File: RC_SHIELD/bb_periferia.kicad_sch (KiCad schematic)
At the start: 29 parts, among them J1 P5a, J2 P4a, J3 FAN, J4 I2C_TEMP, J5 GPIO1, J6 ESTOP, J7 DOOR_SWITCH, J8 GPIO2, J9 SPI, Q1 BSS123, Q2 BSS123, U1 ESP8266-01/ESP-01, U2 SN75LBC179AD, U3 LCD-016N002L

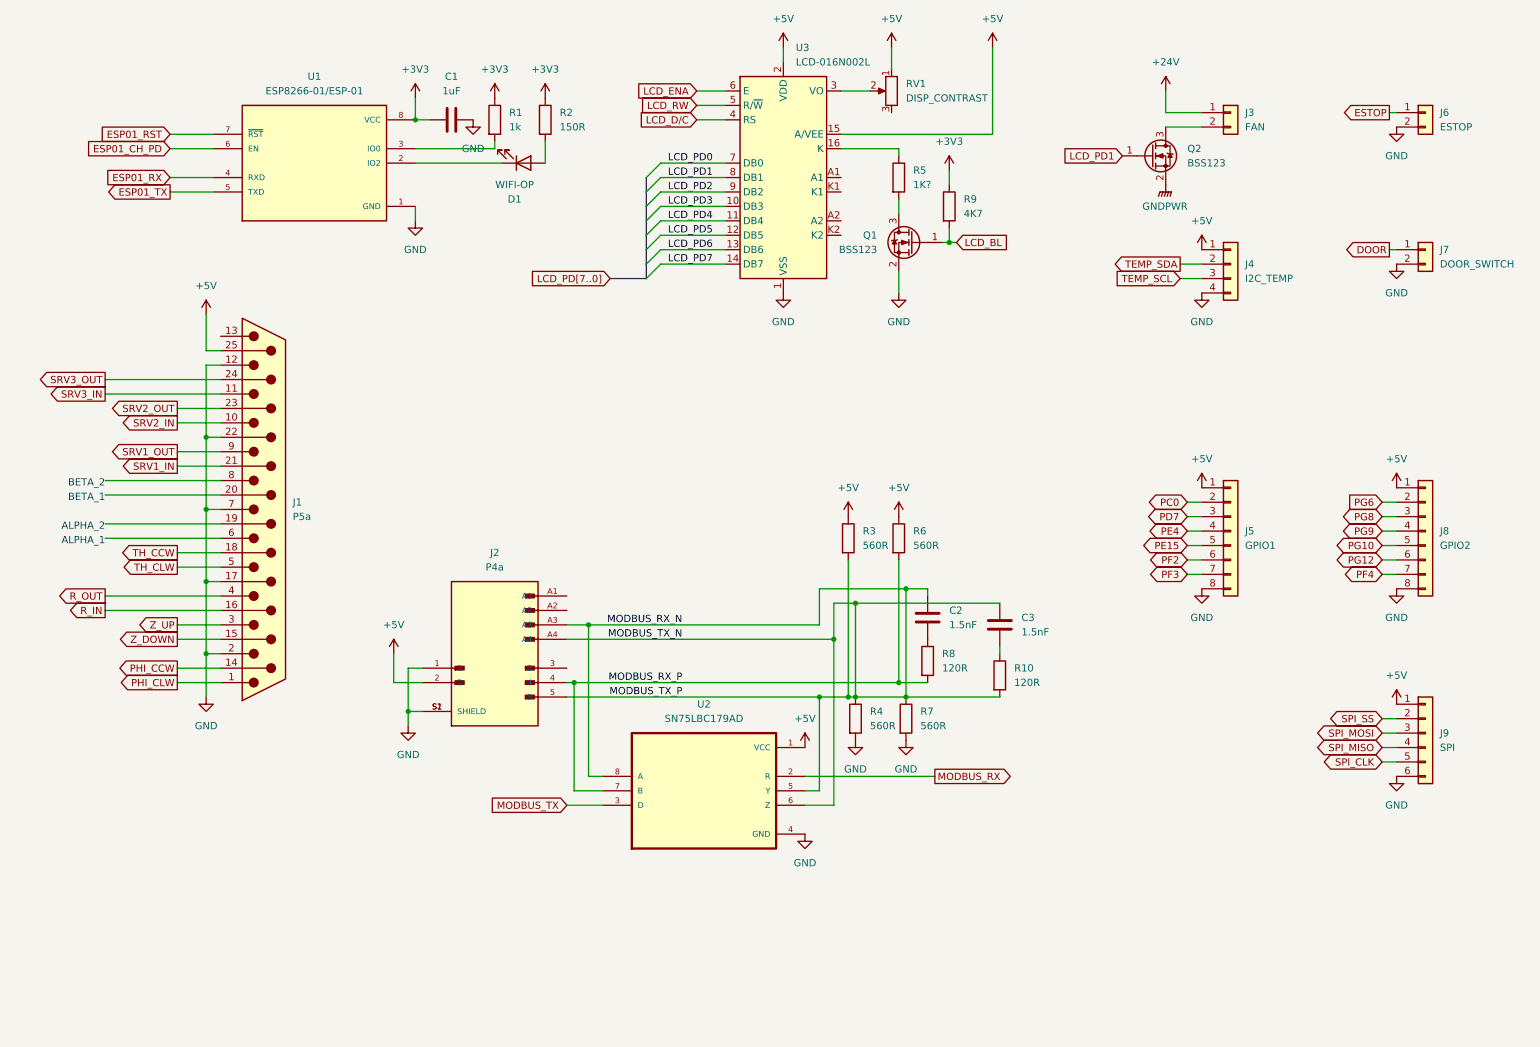
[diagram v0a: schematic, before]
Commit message: added secondary MCU to schematic and made it more consistent
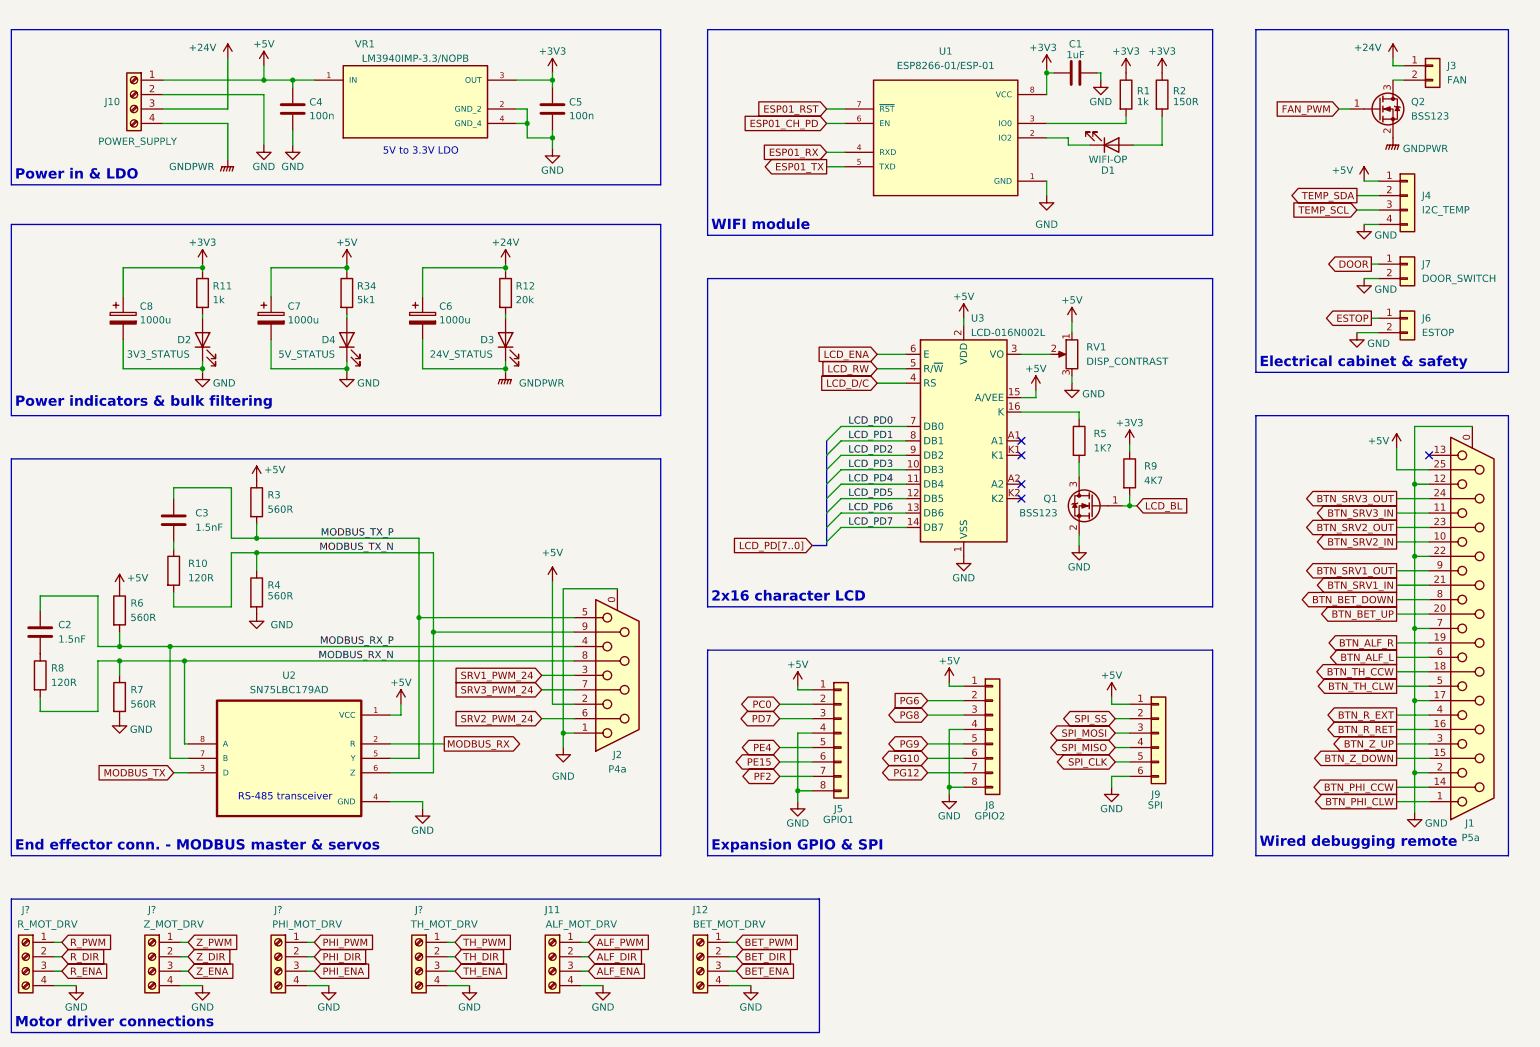
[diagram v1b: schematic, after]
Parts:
- added C4, C5: 100n, symbol Device:C
- added C6, C7, C8: 1000u, symbol Device:C_Polarized
- added D2: 3V3_STATUS, symbol Device:LED
- added D3: 24V_STATUS, symbol Device:LED
- added D4: 5V_STATUS, symbol Device:LED
- added J10: POWER_SUPPLY, symbol Connector:Screw_Terminal_01x04
- added J11: ALF_MOT_DRV, symbol Connector:Screw_Terminal_01x04
- added J12: BET_MOT_DRV, symbol Connector:Screw_Terminal_01x04
- added J?: TH_MOT_DRV, symbol Connector:Screw_Terminal_01x04
- added J?: PHI_MOT_DRV, symbol Connector:Screw_Terminal_01x04
- added J?: Z_MOT_DRV, symbol Connector:Screw_Terminal_01x04
- added J?: R_MOT_DRV, symbol Connector:Screw_Terminal_01x04
- added R11: 1k, symbol Device:R
- added R12: 20k, symbol Device:R
- added R34: 5k1, symbol Device:R
- added VR1: LM3940IMP-3.3/NOPB, LM3940IMP-3.3/NOPB:VREG_LM3940IMP-3.3/NOPB, symbol LM3940IMP-3.3_NOPB:LM3940IMP-3.3/NOPB
- J1: symbol Connector:DB25_Plug -> Connector:DB25_Receptacle_MountingHoles
- J2: symbol DB9W4P500H30LF:DB9W4P500H30LF -> Connector:DE9_Receptacle_MountingHoles
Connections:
- net PF3 is gone; now on net PF2: J5.7 (Pin_7)
- net PF4 is gone; now on net PG12: J8.7 (Pin_7)
- net +24V: now also C6.1, J10.3 (Pin_3), R12.1
- net +3V3: now also C5.1, C8.1, R11.1, VR1.3 (OUT)
- net +5V: now also C4.1, C7.1, J10.1 (Pin_1), R34.1, VR1.1 (IN)
- net GND: now also J1.0 (PAD), J2.0 (PAD), J5.4 (Pin_4), J8.4 (Pin_4), RV1.3, C4.2, C5.2, C7.2, C8.2, D2.1 (K), D4.1 (K), J10.2 (Pin_2), J11.4 (Pin_4), J12.4 (Pin_4), J?.4 (Pin_4), J?.4 (Pin_4), J?.4 (Pin_4), J?.4 (Pin_4), VR1.2 (GND_2), VR1.4 (GND_4); no longer J2.S1 (SHIELD), J2.S2 (SHIELD)
- net GNDPWR: now also C6.2, D3.1 (K), J10.4 (Pin_4)
- net LCD_PD1: no longer Q2.1 (G)
- net MODBUS_RX_N: now also J2.8, R8.2; no longer C2.1, C3.1, J2.5, J2.A3, J2.A4, R10.2, R3.2, R4.1, U2.5 (Y), U2.6 (Z)
- net MODBUS_RX_P: now also C2.1; no longer R8.2
- net PE15: now also J5.6 (Pin_6); no longer J5.5 (Pin_5)
- net PE4: now also J5.5 (Pin_5); no longer J5.4 (Pin_4)
- net PF2: no longer J5.6 (Pin_6)
- net PG10: now also J8.6 (Pin_6); no longer J8.5 (Pin_5)
- net PG12: no longer J8.6 (Pin_6)
- net PG9: now also J8.5 (Pin_5); no longer J8.4 (Pin_4)
- net BTN_ALF_R: now reaches J1.19 (P19)
- net BTN_BET_UP: now reaches J1.20 (P20)
- net BTN_ALF_L: now reaches J1.6
- net BTN_BET_DOWN: now reaches J1.8
- net SRV1_PWM_24: now reaches J2.3
- net PHI_CCW renamed BTN_PHI_CCW
- net PHI_CLW renamed BTN_PHI_CLW
- net R_IN renamed BTN_R_RET
- net R_OUT renamed BTN_R_EXT
- net SRV1_IN renamed BTN_SRV1_IN
- net SRV1_OUT renamed BTN_SRV1_OUT
- net SRV2_IN renamed BTN_SRV2_IN
- net SRV2_OUT renamed BTN_SRV2_OUT
- net SRV3_IN renamed BTN_SRV3_IN
- net SRV3_OUT renamed BTN_SRV3_OUT
- net TH_CCW renamed BTN_TH_CCW
- net TH_CLW renamed BTN_TH_CLW
- net Z_DOWN renamed BTN_Z_DOWN
- net Z_UP renamed BTN_Z_UP
- new net: D4.2 (A), R34.2
- new net: D3.2 (A), R12.2
- new net: D2.2 (A), R11.2
- new net ALF_DIR: J11.2 (Pin_2)
- new net ALF_ENA: J11.3 (Pin_3)
- new net ALF_PWM: J11.1 (Pin_1)
- new net BET_DIR: J12.2 (Pin_2)
- new net BET_ENA: J12.3 (Pin_3)
- new net BET_PWM: J12.1 (Pin_1)
- new net FAN_PWM: Q2.1 (G)
- new net MODBUS_TX_N: J2.9, R10.2, R4.1, U2.6 (Z)
- new net MODBUS_TX_P: C3.1, J2.5, R3.2, U2.5 (Y)
- new net PHI_DIR: J?.2 (Pin_2)
- new net PHI_ENA: J?.3 (Pin_3)
- new net PHI_PWM: J?.1 (Pin_1)
- new net R_DIR: J?.2 (Pin_2)
- new net R_ENA: J?.3 (Pin_3)
- new net R_PWM: J?.1 (Pin_1)
- new net SRV2_PWM_24: J2.6
- new net SRV3_PWM_24: J2.7
- new net TH_DIR: J?.2 (Pin_2)
- new net TH_ENA: J?.3 (Pin_3)
- new net TH_PWM: J?.1 (Pin_1)
- new net Z_DIR: J?.2 (Pin_2)
- new net Z_ENA: J?.3 (Pin_3)
- new net Z_PWM: J?.1 (Pin_1)
- no-connect marks 0 -> 5
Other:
- note added: "2x16 character LCD"
- note added: "5V to 3.3V LDO"
- note added: "Electrical cabinet & safety"
- note added: "End effector conn. - MODBUS master & servos"
- note added: "Expansion GPIO & SPI"
- note added: "Motor driver connections"
- note added: "Power in & LDO"
- note added: "Power indicators & bulk filtering"
- note added: "RS-485 transceiver"
- note added: "WIFI module"
- note added: "Wired debugging remote"
- note removed: "ALPHA_1"
- note removed: "ALPHA_2"
- note removed: "BETA_1"
- note removed: "BETA_2"
- company: (none) -> LEGO Kör (legokor.hu)
- title: PERIFERIA -> Karcsi (INDACT Robot Arm) - Power & peripherals
- moved on the sheet: C1, C2, C3, D1, J3, J4, J5, J6, J7, J8, J9, Q1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

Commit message: Added testpoints
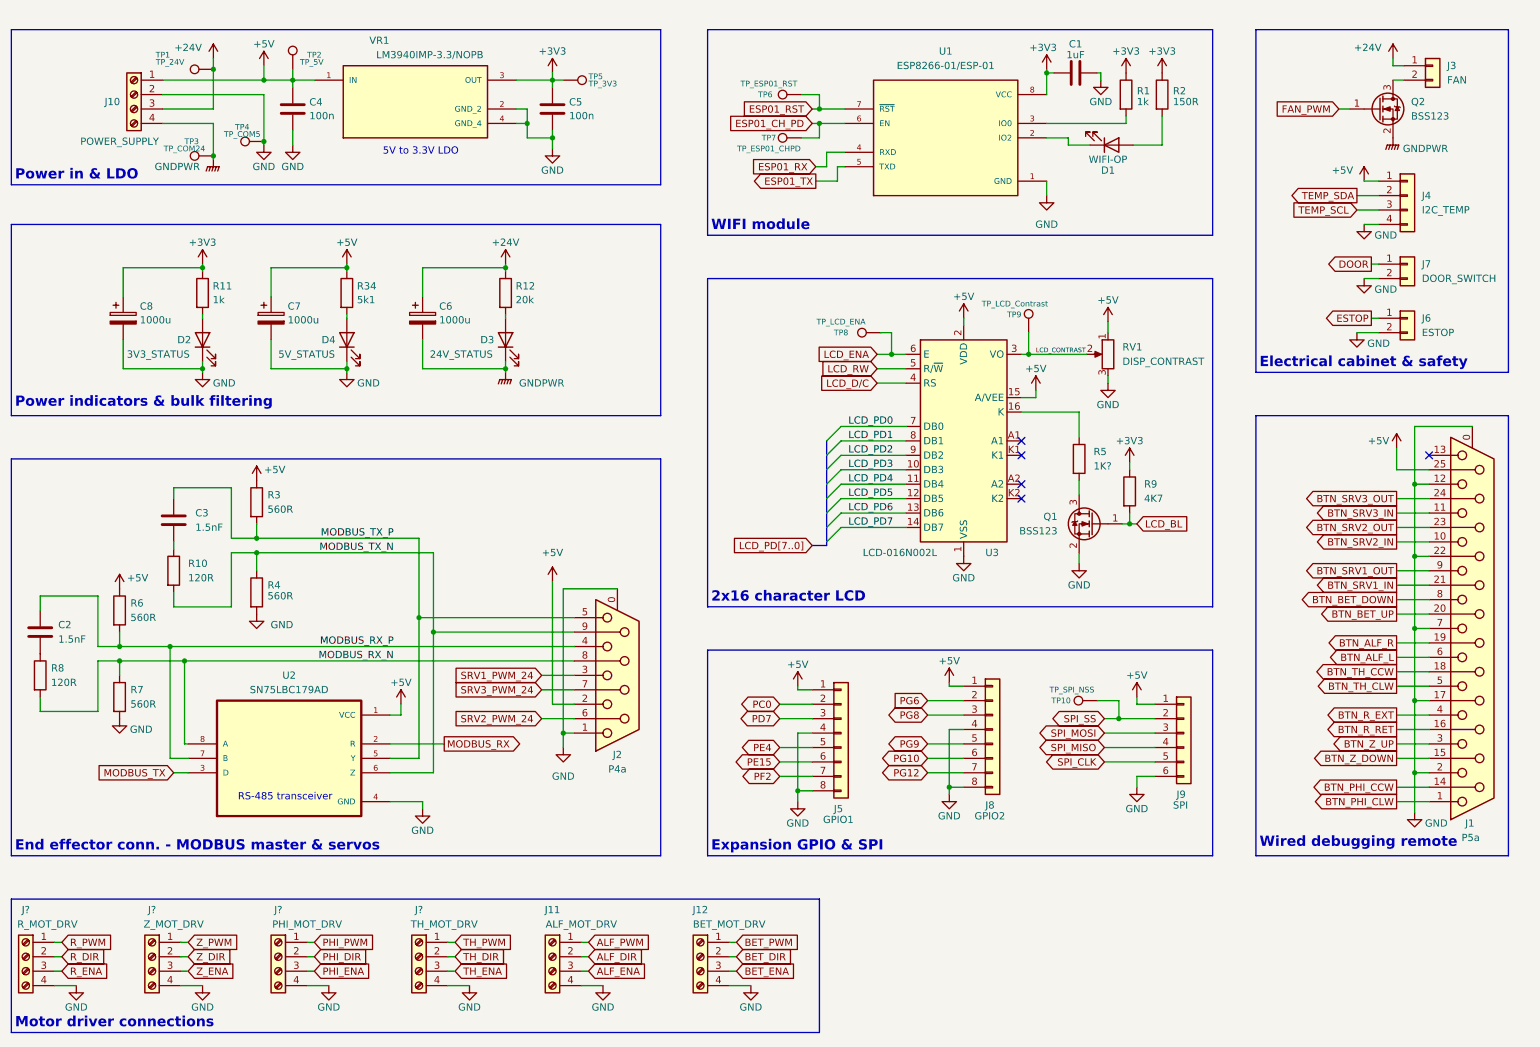
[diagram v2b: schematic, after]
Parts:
- added TP1: TP_24V, symbol Connector:TestPoint
- added TP10: TP_SPI_NSS, symbol Connector:TestPoint
- added TP2: TP_5V, symbol Connector:TestPoint
- added TP3: TP_COM24, symbol Connector:TestPoint
- added TP4: TP_COM5, symbol Connector:TestPoint
- added TP5: TP_3V3, symbol Connector:TestPoint
- added TP6: TP_ESP01_RST, symbol Connector:TestPoint
- added TP7: TP_ESP01_CHPD, symbol Connector:TestPoint
- added TP8: TP_LCD_ENA, symbol Connector:TestPoint
- added TP9: TP_LCD_Contrast, symbol Connector:TestPoint
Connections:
- net +24V: now also TP1.1
- net +3V3: now also TP5.1
- net +5V: now also TP2.1
- net ESP01_CH_PD: now also TP7.1
- net ESP01_RST: now also TP6.1
- net GND: now also TP4.1
- net GNDPWR: now also TP3.1
- net LCD_ENA: now also TP8.1
- net SPI_SS: now also TP10.1
- net LCD_CONTRAST: now reaches RV1.2, U3.3 (VO)
- net LCD_CONTRAST: now also TP9.1
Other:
- moved on the sheet: J9, Q1, R5, R9, RV1

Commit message: footprints assigned
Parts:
- C1: value 1uF -> 1u; footprint (none) -> Capacitor_SMD:C_0805_2012Metric_Pad1.18x1.45mm_HandSolder
- C2, C3: value 1.5nF -> 1.5n; footprint (none) -> Capacitor_SMD:C_0805_2012Metric_Pad1.18x1.45mm_HandSolder
- C4, C5, D1, D2, D3, D4: footprint (none) -> Capacitor_SMD:C_0805_2012Metric_Pad1.18x1.45mm_HandSolder
- C6, C7, C8: footprint (none) -> Capacitor_SMD:CP_Elec_16x22
- J1: footprint (none) -> Connector_Dsub:DSUB-25_Female_Horizontal_P2.77x2.84mm_EdgePinOffset7.70mm_Housed_MountingHolesOffset9.12mm
- J10, J11, J12, J? (x4): footprint (none) -> TerminalBlock_4Ucon:TerminalBlock_4Ucon_1x04_P3.50mm_Horizontal
- J2: footprint DB9W4P500H30LF:AMPHENOL_DB9W4P500H30LF -> Connector_Dsub:DSUB-9_Female_Horizontal_P2.77x2.84mm_EdgePinOffset4.94mm_Housed_MountingHolesOffset7.48mm
- J3, J6, J7: footprint (none) -> Connector_PinHeader_2.54mm:PinHeader_1x02_P2.54mm_Vertical
- J4: footprint (none) -> Connector_PinHeader_2.54mm:PinHeader_1x04_P2.54mm_Vertical
- J5, J8: footprint (none) -> Connector_PinHeader_2.54mm:PinHeader_1x08_P2.54mm_Vertical
- J9: footprint (none) -> Connector_PinHeader_2.54mm:PinHeader_1x06_P2.54mm_Vertical
- R1, R10, R11, R12, R2, R3, R34, R4, R5, R6, R7, R8, R9: footprint (none) -> Resistor_SMD:R_0805_2012Metric_Pad1.20x1.40mm_HandSolder
- RV1: footprint (none) -> Potentiometer_SMD:Potentiometer_Vishay_TS53YJ_Vertical
- TP1, TP10, TP2, TP3, TP4, TP5, TP6, TP7, TP8, TP9: footprint (none) -> TestPoint:TestPoint_Pad_2.0x2.0mm
- U1: footprint ESP8266-01/ESP-01:XCVR_ESP8266-01/ESP-01 -> ESP-01:XCVR_ESP8266-01_ESP-01
- VR1: footprint LM3940IMP-3.3/NOPB:VREG_LM3940IMP-3.3/NOPB -> LM3940IMP-3:VREG_LM3940IMP-3.3_NOPB

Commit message: Fixed typos and names in schematic, changed optocoupler resistors; added .gitgnore file
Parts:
- J11: renamed from J5; symbol Connector_Generic:Conn_01x08 -> Connector_Generic:Conn_01x07
- J12: renamed from J8; symbol Connector_Generic:Conn_01x08 -> Connector_Generic:Conn_01x07
- U4: renamed from U3; footprint Display:LCD-016N002L -> Connector_PinHeader_2.54mm:PinHeader_1x16_P2.54mm_Horizontal
- renumbered C3 to C11, C1 to C16, C2 to C9, D1 to D4, J9 to J13, J4 to J14, J7 to J15, J6 to J16, J3 to J17, J1 to J18, J2 to J9, R5 to R11, R1 to R12, R9 to R13, R2 to R14, R8 to R2, R6 to R3, R7 to R4, R10 to R5, R3 to R7, R4 to R8, TP3 to TP2, TP4 to TP3, TP2 to TP4, U1 to U3
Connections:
- net PG8 is gone; now on net PG6: J12.3 (Pin_3)
- net PG9 is gone; now on net PG10: J12.5 (Pin_5)
- net GND: now also J11.7 (Pin_7), J12.7 (Pin_7); no longer J11.8 (Pin_8), J12.8 (Pin_8)
- net PF2: now also J12.2 (Pin_2); no longer J11.7 (Pin_7)
- net PG10: no longer J12.6 (Pin_6)
- net PG12: now also J12.6 (Pin_6); no longer J12.7 (Pin_7)
- net PG6: no longer J12.2 (Pin_2)
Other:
- moved on the sheet: C11, C16, C4, C5, C6, C7, C8, C9, D2, D3, D4, J10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

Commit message: created pcb layout, review needed
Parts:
- J11, J12: footprint Connector_PinHeader_2.54mm:PinHeader_1x08_P2.54mm_Vertical -> Connector_PinHeader_2.54mm:PinHeader_1x07_P2.54mm_Vertical
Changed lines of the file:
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@@
       (effects (font (size 1.27 1.27)) (justify left))
     )
-    (property "Footprint" "Connector_PinHeader_2.54mm:PinHeader_1x08_P2.54mm_Vertical" (at 162.56 140.335 0)
+    (property "Footprint" "Connector_PinHeader_2.54mm:PinHeader_1x07_P2.54mm_Vertical" (at 162.56 140.335 0)
       (effects (font (size 1.27 1.27)) hide)
     )
@@
       (effects (font (size 1.27 1.27)) (justify left))
     )
-    (property "Footprint" "Connector_PinHeader_2.54mm:PinHeader_1x08_P2.54mm_Vertical" (at 189.23 139.7 0)
-      (effects (font (size 1.27 1.27)) hide)
-    )
+    (property "Footprint" "Connector_PinHeader_2.54mm:PinHeader_1x07_P2.54mm_Vertical" (at 189.23 139.7 0)
+      (effects (font (size 1.27 1.27)) hide)
+    )

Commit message: final fixes
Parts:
- C4: value 100n -> 470n
- C5: value 100n -> 33u
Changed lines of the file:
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@@
   (symbol (lib_id "Device:C") (at 111.76 30.48 0) (unit 1)
     (in_bom yes) (on_board yes) (dnp no) (fields_autoplaced)
-    (property "Reference" "C5" (at 114.681 29.2679 0)
-      (effects (font (size 1.27 1.27)) (justify left))
-    )
-    (property "Value" "100n" (at 114.681 31.6921 0)
+    (property "Reference" "C5" (at 115.57 29.21 0)
+      (effects (font (size 1.27 1.27)) (justify left))
+    )
+    (property "Value" "33u" (at 115.57 31.75 0)
       (effects (font (size 1.27 1.27)) (justify left))
     )
@@
   (symbol (lib_id "Device:C") (at 66.04 30.48 0) (unit 1)
     (in_bom yes) (on_board yes) (dnp no) (fields_autoplaced)
-    (property "Reference" "C4" (at 68.961 29.2679 0)
-      (effects (font (size 1.27 1.27)) (justify left))
-    )
-    (property "Value" "100n" (at 68.961 31.6921 0)
-      (effects (font (size 1.27 1.27)) (justify left))
-    )
+    (property "Reference" "C4" (at 69.85 29.21 0)
+      (effects (font (size 1.27 1.27)) (justify left))
+    )
+    (property "Value" "470n" (at 69.85 31.75 0)
+      (effects (font (size 1.27 1.27)) (justify left))
+    )
